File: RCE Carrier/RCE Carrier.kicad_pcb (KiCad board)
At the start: 2 copper layers, 38 x 39.5 mm, 35 parts, among them J10 Conn_01x06_Pin, J11 Conn_01x02, J2 XT60PW-F, J3 XT30UPB-M, J4 XT60PW-F, J5 DF40C-34DP-0.4V_58_, J6 PRT-16766, J7 DF40C-34DP-0.4V_58_, J9 XT30UPB-M, U2 TPS54302DDCR, U3 BD6222HFP-TR, U4 LMR51430, U5 BD6222HFP-TR

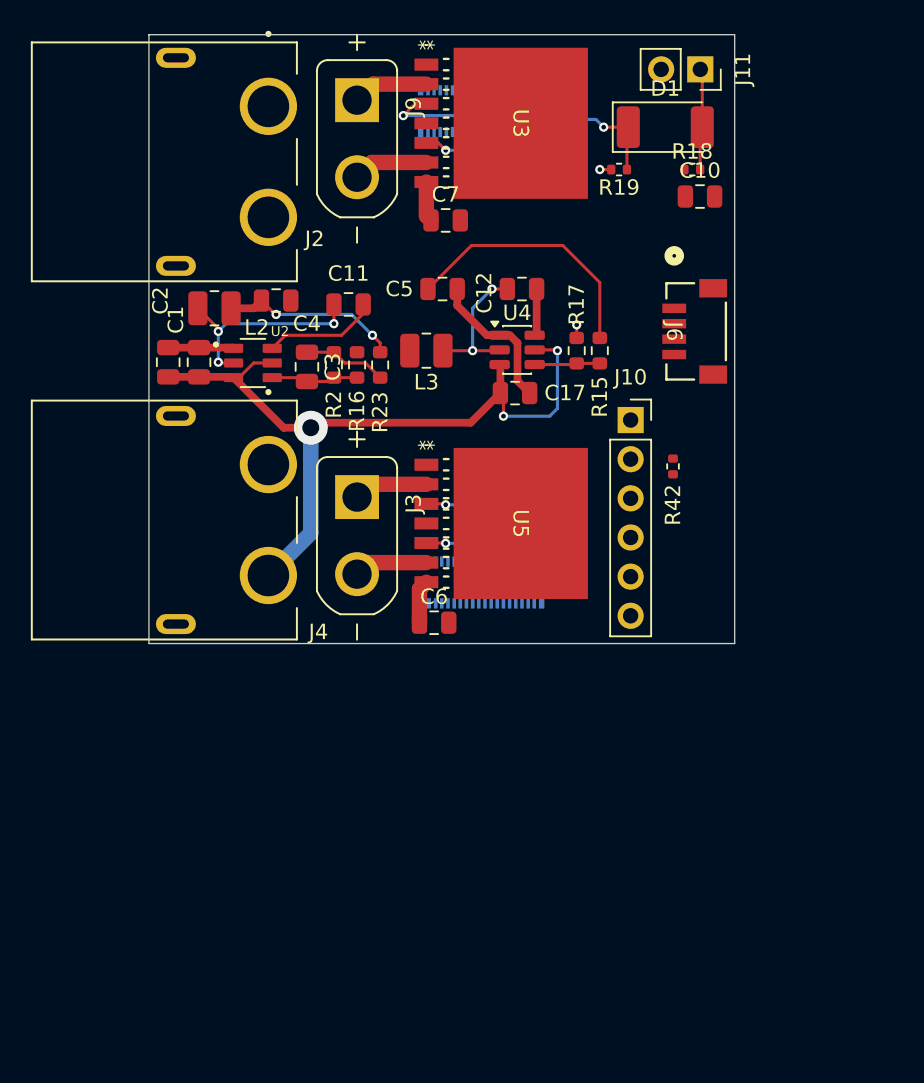
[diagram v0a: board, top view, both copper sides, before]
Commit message: split pce and rce functions into two carriers, initial rce parts placement
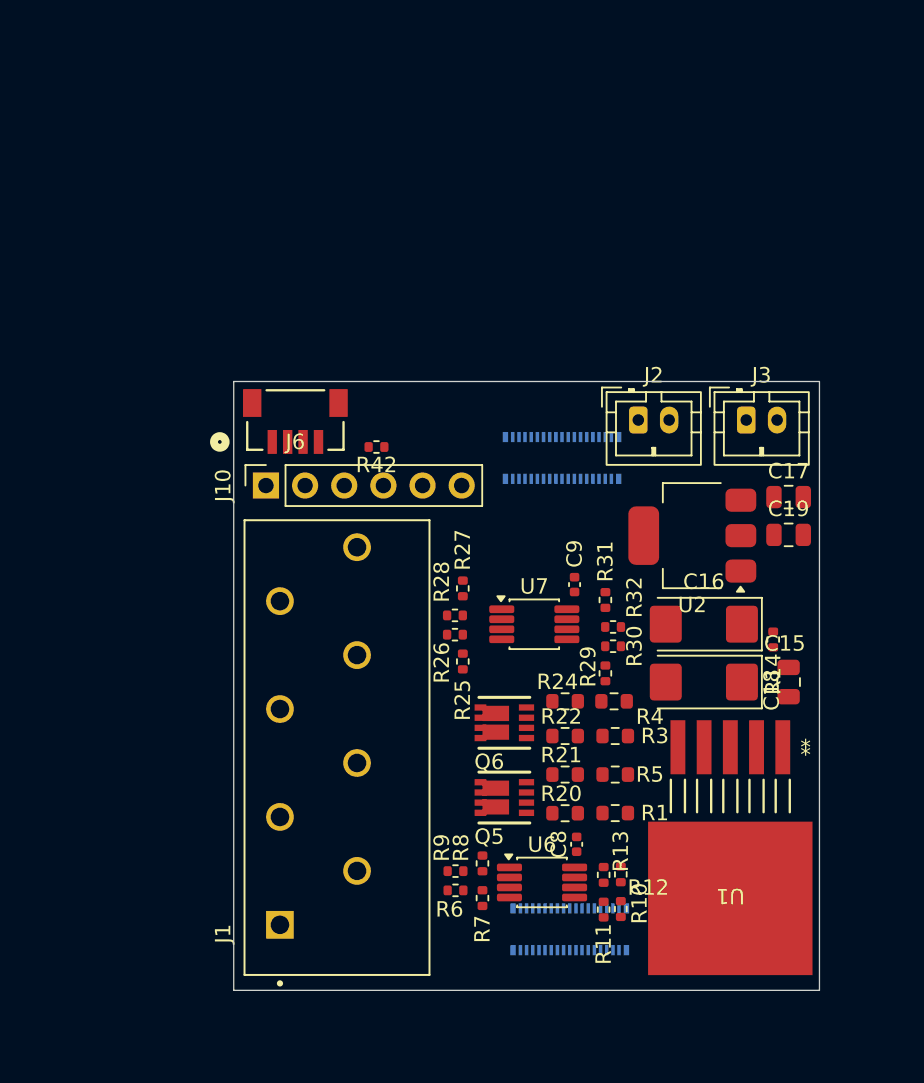
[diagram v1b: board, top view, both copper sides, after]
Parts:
- removed C1, C6, C7: 10u, Capacitor_SMD:C_0805_2012Metric
- removed C10: 2.2u, Capacitor_SMD:C_0805_2012Metric
- removed C11: 0.1u 16V, Capacitor_SMD:C_0805_2012Metric
- removed C12, C2: 0.1u, Capacitor_SMD:C_0805_2012Metric
- removed C3: 56p, Capacitor_SMD:C_0805_2012Metric
- removed C4: 44u, Capacitor_SMD:C_0805_2012Metric
- removed C5: 44u 25V, Capacitor_SMD:C_0805_2012Metric
- removed D1: SM4004, Diode_SMD:D_MELF
- removed J11: Conn_01x02, Connector_PinSocket_2.54mm:PinSocket_1x02_P2.54mm_Vertical
- removed J4: XT60PW-F, XT60PW-F:AMASS_XT60PW-F
- removed J9: XT30UPB-M, XT30UPB-M:AMASS_XT30UPB-M
- removed L2, L3: 6.8u, Inductor_SMD:L_1008_2520Metric
- removed R15: 100k 1%, Resistor_SMD:R_0603_1608Metric
- removed R16: 22.1k, Resistor_SMD:R_0603_1608Metric
- removed R17: 5.23k 1%, Resistor_SMD:R_0603_1608Metric
- removed R18: 1k, Resistor_SMD:R_0402_1005Metric
- removed R19: 1M, Resistor_SMD:R_0402_1005Metric
- removed R2: 100k, Resistor_SMD:R_0603_1608Metric
- removed R23: 49.9, Resistor_SMD:R_0603_1608Metric
- removed U3, U5: BD6222HFP-TR, BD6222HFP-TR:HRP7_ROM
- removed U4: LMR51430, Package_TO_SOT_SMD:SOT-23-6
- added C15: 1u, Capacitor_SMD:C_0805_2012Metric, F.Cu at (163.5, 96.0)
- added C16: 47u, Capacitor_Tantalum_SMD:CP_EIA-6032-28_Kemet-C, F.Cu at (158.0, 92.2)
- added C18: 47u, Capacitor_Tantalum_SMD:CP_EIA-6032-28_Kemet-C, F.Cu at (158.0, 96.0)
- added C19: 10u, Capacitor_SMD:C_0805_2012Metric, F.Cu at (163.5, 86.5)
- added C8: 100n, Capacitor_SMD:C_0402_1005Metric, F.Cu at (149.8, 106.5)
- added C9: 100n, Capacitor_SMD:C_0402_1005Metric, F.Cu at (149.6, 89.7)
- added J1: TBL002A-350-08GY-2GY, TBL002A-350-08GY-2GY:CUI_TBL002A-350-08GY-2GY, F.Cu at (130.5, 111.8)
- added Q5: SI7232DN-T1-GE3, Si7232DN:TRANS_SI7232DN-T1-GE3, F.Cu at (145.1, 103.5)
- added Q6: SI7232DN-T1-GE3, Si7232DN:TRANS_SI7232DN-T1-GE3, F.Cu at (145.1, 98.6)
- added R1: 3.3k, Resistor_SMD:R_0603_1608Metric, F.Cu at (152.2, 104.5)
- added R10: 10k 1%, Resistor_SMD:R_0402_1005Metric, F.Cu at (152.6, 110.7)
- added R11: 8.06k 1%, Resistor_SMD:R_0402_1005Metric, F.Cu at (151.5, 110.8)
- added R12: 10k 1%, Resistor_SMD:R_0402_1005Metric, F.Cu at (152.6, 108.5)
- added R13: 9.09k 1%, Resistor_SMD:R_0402_1005Metric, F.Cu at (151.5, 108.5)
- added R14: 10k, Resistor_SMD:R_0402_1005Metric, F.Cu at (162.5, 93.2)
- added R20: 100, Resistor_SMD:R_0603_1608Metric, F.Cu at (149.0, 104.5)
- added R21: 100, Resistor_SMD:R_0603_1608Metric, F.Cu at (149.0, 102.0)
- added R22: 100, Resistor_SMD:R_0603_1608Metric, F.Cu at (149.0, 99.5)
- added R24: 100, Resistor_SMD:R_0603_1608Metric, F.Cu at (149.0, 97.2)
- added R25: 10k 1%, Resistor_SMD:R_0402_1005Metric, F.Cu at (142.4, 94.7)
- added R26: 8.06k 1%, Resistor_SMD:R_0402_1005Metric, F.Cu at (141.9, 92.9)
- added R27: 10k 1%, Resistor_SMD:R_0402_1005Metric, F.Cu at (142.4, 89.9)
- added R28: 9.09k 1%, Resistor_SMD:R_0402_1005Metric, F.Cu at (141.9, 91.7)
- added R29: 10k 1%, Resistor_SMD:R_0402_1005Metric, F.Cu at (151.6, 95.4)
- added R3: 1k, Resistor_SMD:R_0603_1608Metric, F.Cu at (152.2, 99.5)
- added R30: 8.06k 1%, Resistor_SMD:R_0402_1005Metric, F.Cu at (152.1, 93.7)
- added R31: 10k 1%, Resistor_SMD:R_0402_1005Metric, F.Cu at (151.6, 90.7)
- added R32: 9.09k 1%, Resistor_SMD:R_0402_1005Metric, F.Cu at (152.1, 92.4)
- added R4: 1k, Resistor_SMD:R_0603_1608Metric, F.Cu at (152.2, 97.2)
- added R5: 1k, Resistor_SMD:R_0603_1608Metric, F.Cu at (152.2, 102.0)
- added R6: 10k 1%, Resistor_SMD:R_0402_1005Metric, F.Cu at (141.9, 109.5)
- added R7: 8.06k 1%, Resistor_SMD:R_0402_1005Metric, F.Cu at (143.6, 110.0)
- added R8: 9.09k 1%, Resistor_SMD:R_0402_1005Metric, F.Cu at (143.6, 107.8)
- added R9: 10k 1%, Resistor_SMD:R_0402_1005Metric, F.Cu at (141.9, 108.3)
- added U1: TPS75533KTTRG3, TPS75533KTTRG3:KTT5_6P22X6P86, F.Cu at (159.7, 109.9)
- added U6: LM293, Package_SO:VSSOP-8_3x3mm_P0.65mm, F.Cu at (147.5, 109.0)
- added U7: LM293, Package_SO:VSSOP-8_3x3mm_P0.65mm, F.Cu at (147.0, 92.2)
- C17: value 2.2u -> 10u
- J2: value XT60PW-F -> Conn_01x02; footprint XT60PW-F:AMASS_XT60PW-F -> Connector_JST:JST_PH_B2B-PH-K_1x02_P2.00mm_Vertical
- J3: value XT30UPB-M -> Conn_01x02; footprint XT30UPB-M:AMASS_XT30UPB-M -> Connector_JST:JST_PH_B2B-PH-K_1x02_P2.00mm_Vertical
- J6: footprint I2C-QWIIC-CONN:CONN_BM04B-SRSS-TB_SPK -> i2c_qwiic_connector:CONN_BM04B-SRSS-TB_SPK
- U2: value TPS54302DDCR -> NCP1117-3.3_SOT223; footprint TPS54302DDCR:SOT95P280X110-6N -> Package_TO_SOT_SMD:SOT-223-3_TabPin2
- moved U2 30.6 mm to (157.2, 86.5), turned to 180 degrees
- moved J2 29.3 mm to (153.8, 79.0), turned to 0 degrees
- moved J6 26.6 mm to (131.5, 79.0), turned to 0 degrees
- moved J3 26.3 mm to (160.8, 79.0), turned to 0 degrees
- moved J10 24.0 mm to (129.6, 83.2), turned to 90 degrees
- moved J7 23.2 mm to (149.3, 112.0)
- moved J5 23.2 mm to (148.8, 81.5)
- moved R42 19.3 mm to (136.8, 80.8), turned to 180 degrees
- moved C17 19.0 mm to (163.5, 84.0)
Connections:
- C17 pad 1: VIN -> +3V7_LIPO
- J2 pad 1: /Power Distribution and Motor Control/VBAT -> /Power Distribution/VBAT
- J5 pad 14: /PAYLOAD_1F -> unconnected-(J5-Pad14)
- J5 pad 16: /PAYLOAD_1R -> unconnected-(J5-Pad16)
- J5 pad 28: /PAYLOAD_A -> unconnected-(J5-Pad28)
- J7 pad 16: unconnected-(J7-Pad16) -> +3V3_REG
- J7 pad 20: unconnected-(J7-Pad20) -> +3V3_REG
- J7 pad 21: /PAYLOAD_2R -> unconnected-(J7-Pad21)
- J7 pad 23: /PAYLOAD_2F -> unconnected-(J7-Pad23)
- J7 pad 24: unconnected-(J7-Pad24) -> +3V3_REG
- J7 pad 28: unconnected-(J7-Pad28) -> +3V3_REG
- U2 pad 2: Net-(U2-SW) -> +3V3_REG
- U2 pad 3: VIN -> +3V7_LIPO
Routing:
- net VIN: track 49.9 -> 0.00 mm, vias 3 -> 0
- net +12V: track 22.3 -> 0.00 mm
- net GND: track 15.4 -> 0.00 mm, vias 2 -> 0
- net Net-(U2-SW): track 14.0 -> 0.00 mm, vias 3 -> 0
- net +3V3_REG: track 11.6 -> 0.00 mm, vias 2 -> 0
- net /PAYLOAD_A: track 11.5 -> 0.00 mm, vias 1 -> 0
- net Net-(U4-SW): track 9.21 -> 0.00 mm, vias 2 -> 0
- net Net-(U2-BOOT): track 7.43 -> 0.00 mm
- net /PAYLOAD_2F: track 6.97 -> 0.00 mm, vias 1 -> 0
- net Net-(D1-A): track 6.61 -> 0.00 mm
- net /PAYLOAD_1F: track 6.59 -> 0.00 mm, vias 1 -> 0
- net Net-(U2-FB): track 5.71 -> 0.00 mm
- net Net-(C3-Pad1): track 5.43 -> 0.00 mm
- net /PAYLOAD_2R: track 5.42 -> 0.00 mm, vias 1 -> 0
- net /Power Distribution and Motor Control/MOTOR1A: track 4.93 -> 0.00 mm
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
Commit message: RCE wiring except 3V3 in
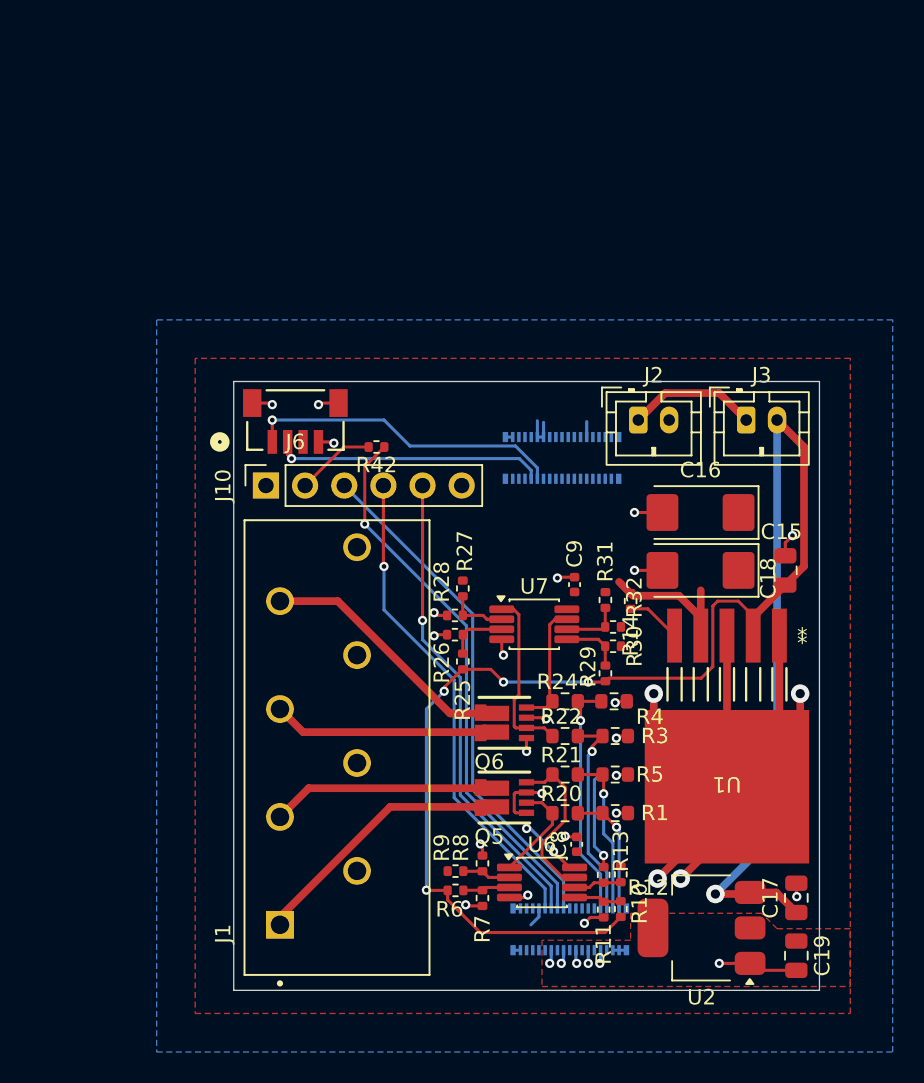
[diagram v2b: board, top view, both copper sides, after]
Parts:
- moved C19 27.3 mm to (164.0, 113.8), turned to -90 degrees
- moved C17 26.0 mm to (164.0, 110.0), turned to 90 degrees
- moved U2 25.5 mm to (157.8, 112.0)
- moved R14 9.58 mm to (153.2, 90.7)
- moved C15 7.25 mm to (163.3, 88.8)
- moved C16 7.25 mm to (157.8, 85.0)
- moved C18 7.25 mm to (157.8, 88.8)
- moved U1 7.25 mm to (159.5, 102.6)
- turned R27 to -90 degrees
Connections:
- J6 pad 5: (no net) -> GND
- J6 pad 6: (no net) -> GND
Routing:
- net +3V7_LIPO: track 0.00 -> 109.5 mm, vias 0 -> 5
- net GND: track 0.00 -> 99.2 mm, vias 0 -> 29
- net /MISO: track 0.00 -> 35.6 mm, vias 0 -> 1
- net /MOSI: track 0.00 -> 33.3 mm
- net /SPI_CS: track 0.00 -> 31.8 mm, vias 0 -> 1
- net /SCLK: track 0.00 -> 30.9 mm, vias 0 -> 1
- net /SCL: track 0.00 -> 20.6 mm, vias 0 -> 1
- net /SDA: track 0.00 -> 17.6 mm, vias 0 -> 1
- net Net-(J1-Pad1): track 0.00 -> 17.5 mm
- net Net-(J1-Pad7): track 0.00 -> 17.0 mm
- net /PYRO_4: track 0.00 -> 15.6 mm, vias 0 -> 1
- net Net-(J1-Pad3): track 0.00 -> 14.8 mm
- net Net-(J1-Pad5): track 0.00 -> 14.6 mm
- net +3.3V/BP: track 0.00 -> 14.5 mm, vias 0 -> 2
- net /PYRO_3: track 0.00 -> 13.7 mm, vias 0 -> 1
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- added copper zone on F.Cu, net +3.3V/BP
- added copper zone on F.Cu, net +3V3_REG
- added copper zone on B.Cu, net GND

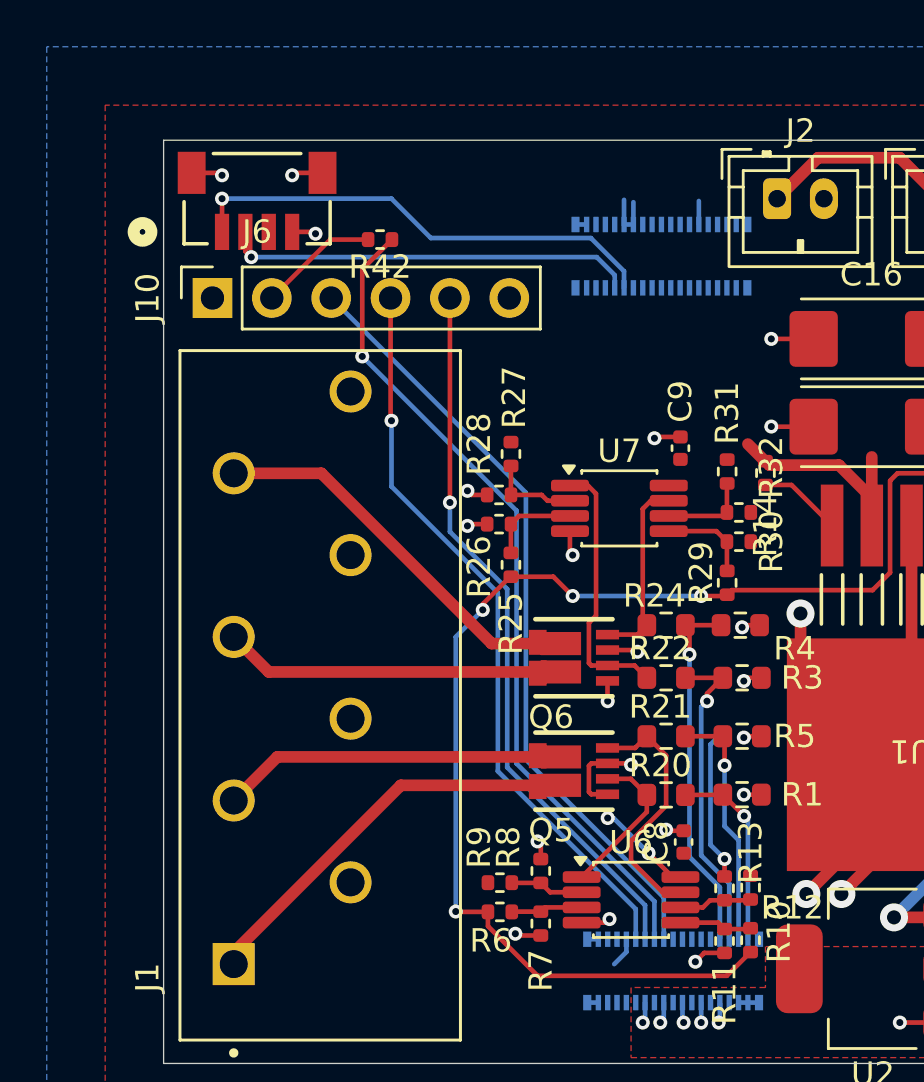
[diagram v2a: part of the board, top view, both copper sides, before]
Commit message: added payload solenoid gpio, 3v3 rail from power mux to carriers, finished wiring
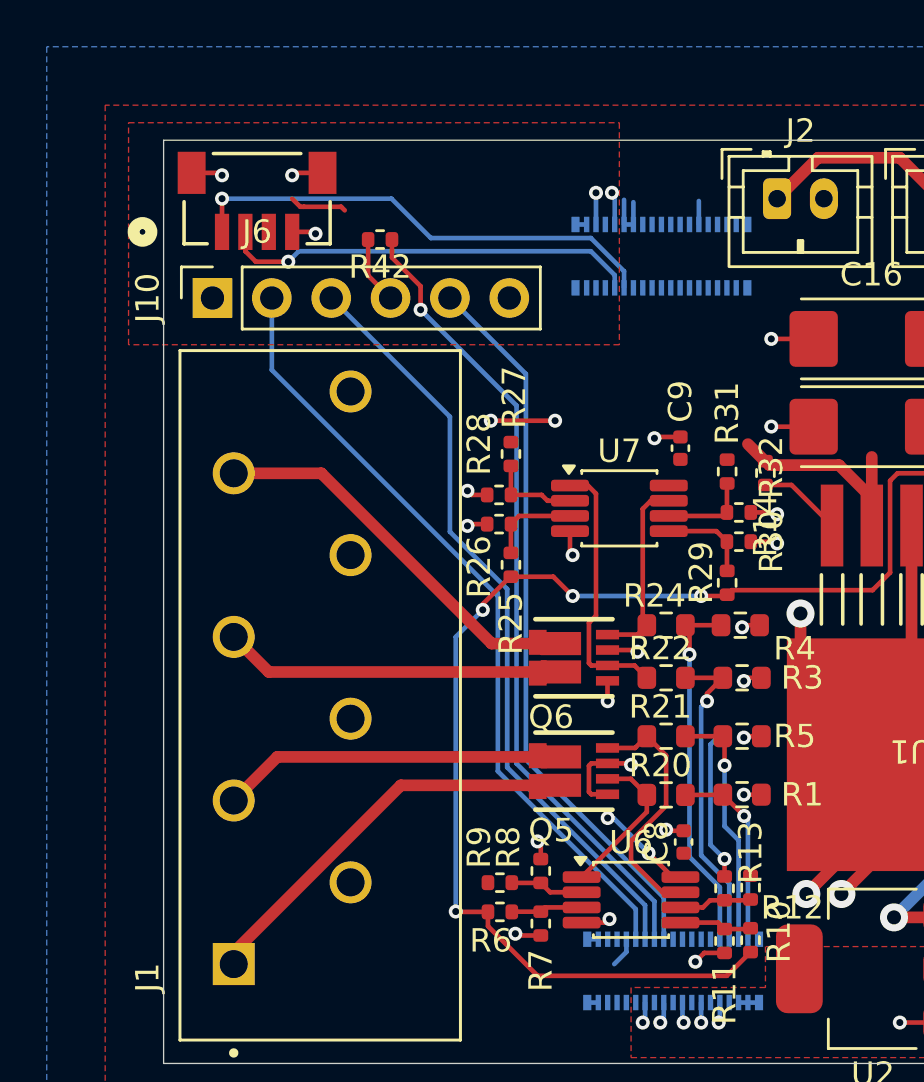
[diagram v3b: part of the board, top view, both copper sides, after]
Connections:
- J10 pad 2: Net-(J10-Pin_2) -> /SPI_CS
- J10 pad 3: /MOSI -> /SCLK
- J10 pad 4: /SPI_CS -> Net-(J10-Pin_4)
- J10 pad 5: /SCLK -> /MOSI
- J5 pad 3: unconnected-(J5-Pad3) -> +3V3
- J5 pad 7: +3V3_REG -> +3V3
- J6 pad 5: GND -> (no net)
- J6 pad 6: GND -> (no net)
- R42 pad 2: Net-(J10-Pin_2) -> Net-(J10-Pin_4)
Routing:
- net +3V3: track 0.00 -> 5.25 mm, vias 0 -> 2
- net Net-(J10-Pin_2): track 5.16 -> 0.00 mm
- net GND: track 99.2 -> 104.3 mm, vias 29 -> 33
- net Net-(J10-Pin_4): track 0.00 -> 2.90 mm
- net /SPI_CS: track 31.8 -> 34.0 mm, vias 1 -> 0
- net /MOSI: track 33.3 -> 31.2 mm
- net /SCLK: track 30.9 -> 33.0 mm, vias 1 -> 0
- net /MISO: track 35.6 -> 34.6 mm
- added copper zone on F.Cu, net +3V3

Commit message: missed an unconnected net
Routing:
- net +3.3V/BP: track 14.5 -> 17.0 mm
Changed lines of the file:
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@@
+	)
+	(segment
+		(start 149.1125 91.275)
+		(end 148.75 90.9125)
+		(width 0.2)
+		(layer "F.Cu")
+		(net "+3.3V{slash}BP")
 	)
 	(segment
@@
 		(end 157.800001 90.050001)
 		(width 0.5)
+		(layer "F.Cu")
+		(net "+3.3V{slash}BP")
+	)
+	(segment
+		(start 148.75 90.9125)
+		(end 148.75 90.25)
+		(width 0.2)
+		(layer "F.Cu")
+		(net "+3.3V{slash}BP")
+	)
+	(segment
+		(start 149.1125 91.275)
+		(end 147.775 91.275)
+		(width 0.2)
 		(layer "F.Cu")
 		(net "+3.3V{slash}BP")
@@
 	)
 	(segment
+		(start 136.25 82.29)
+		(end 137.21 83.25)
+		(width 0.2)
+		(layer "F.Cu")
+		(net "Net-(J10-Pin_4)")
+	)
+	(segment
+		(start 136.25 80.75)
+		(end 136.25 82.29)
+		(width 0.2)
+		(layer "F.Cu")
+		(net "Net-(J10-Pin_4)")
+	)
+	(segment
 		(start 151.415 104.51)
 		(end 151.425 104.5)
@@
 	)
 	(segment
+		(start 141.8 96)
+		(end 132.13 86.33)
+		(width 0.2)
+		(layer "B.Cu")
+		(net "/SPI_CS")
+	)
+	(segment
+		(start 132.13 86.33)
+		(end 132.13 83.25)
+		(width 0.2)
+		(layer "B.Cu")
+		(net "/SPI_CS")
+	)
+	(segment
+		(start 147.7 109.397058)
+		(end 141.8 103.497056)
+		(width 0.2)
+		(layer "B.Cu")
+		(net "/SPI_CS")
+	)
+	(segment
+		(start 141.8 103.497056)
+		(end 141.8 96)
+		(width 0.2)
+		(layer "B.Cu")
+		(net "/SPI_CS")
+	)
+	(segment
+		(start 141.8 96)
+		(end 141.8 95.865686)
+		(width 0.2)
+		(layer "B.Cu")
+		(net "/SPI_CS")
+	)
+	(segment
+		(start 147.7 110.685)
+		(end 147.7 109.397058)
+		(width 0.2)
+		(layer "B.Cu")
+		(net "/SPI_CS")
+	)
+	(segment
+		(start 148.1 110.685)
+		(end 148.1 109.231372)
+		(width 0.2)
+		(layer "B.Cu")
+		(net "/SCLK")
+	)
+	(segment
+		(start 142.2 95.7)
+		(end 139.75 93.25)
+		(width 0.2)
+		(layer "B.Cu")
+		(net "/SCLK")
+	)
+	(segment
+		(start 139.75 88.33)
+		(end 134.67 83.25)
+		(width 0.2)
+		(layer "B.Cu")
+		(net "/SCLK")
+	)
+	(segment
+		(start 148.1 109.231372)
+		(end 142.2 103.331371)
+		(width 0.2)
+		(layer "B.Cu")
+		(net "/SCLK")
+	)
+	(segment
+		(start 142.2 103.331371)
+		(end 142.2 95.7)
+		(width 0.2)
+		(layer "B.Cu")
+		(net "/SCLK")
+	)
+	(segment
+		(start 139.75 93.25)
+		(end 139.75 88.33)
+		(width 0.2)
+		(layer "B.Cu")
+		(net "/SCLK")
+	)
+	(segment
 		(start 148.9 108.9)
 		(end 143 103)
@@
 		(net "/MOSI")
 	)
-	(segment
-		(start 141.8 96)
-		(end 132.13 86.33)
-		(width 0.2)
-		(layer "B.Cu")
-		(net "/SPI_CS")
-	)
-	(segment
-		(start 132.13 86.33)
-		(end 132.13 83.25)
-		(width 0.2)
-		(layer "B.Cu")
-		(net "/SPI_CS")
-	)
-	(segment
-		(start 147.7 109.397058)
-		(end 141.8 103.497056)
-		(width 0.2)
-		(layer "B.Cu")
-		(net "/SPI_CS")
-	)
-	(segment
-		(start 141.8 103.497056)
-		(end 141.8 96)
-		(width 0.2)
-		(layer "B.Cu")
-		(net "/SPI_CS")
-	)
-	(segment
-		(start 141.8 96)
-		(end 141.8 95.865686)
-		(width 0.2)
-		(layer "B.Cu")
-		(net "/SPI_CS")
-	)
-	(segment
-		(start 147.7 110.685)
-		(end 147.7 109.397058)
-		(width 0.2)
-		(layer "B.Cu")
-		(net "/SPI_CS")
-	)
-	(segment
-		(start 148.1 110.685)
-		(end 148.1 109.231372)
-		(width 0.2)
-		(layer "B.Cu")
-		(net "/SCLK")
-	)
-	(segment
-		(start 142.2 95.7)
-		(end 139.75 93.25)
-		(width 0.2)
-		(layer "B.Cu")
-		(net "/SCLK")
-	)
-	(segment
-		(start 139.75 88.33)
-		(end 134.67 83.25)
-		(width 0.2)
-		(layer "B.Cu")
-		(net "/SCLK")
-	)
-	(segment
-		(start 148.1 109.231372)
-		(end 142.2 103.331371)
-		(width 0.2)
-		(layer "B.Cu")
-		(net "/SCLK")
-	)
-	(segment
-		(start 142.2 103.331371)
-		(end 142.2 95.7)
-		(width 0.2)
-		(layer "B.Cu")
-		(net "/SCLK")
-	)
-	(segment
-		(start 139.75 93.25)
-		(end 139.75 88.33)
-		(width 0.2)
-		(layer "B.Cu")
-		(net "/SCLK")
-	)
-	(segment
-		(start 136.25 82.29)
-		(end 137.21 83.25)
-		(width 0.2)
-		(layer "F.Cu")
-		(net "Net-(J10-Pin_4)")
-	)
-	(segment
-		(start 136.25 80.75)
-		(end 136.25 82.29)
-		(width 0.2)
-		(layer "F.Cu")
-		(net "Net-(J10-Pin_4)")
-	)
 	(zone
